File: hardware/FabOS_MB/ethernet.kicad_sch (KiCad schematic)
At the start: 40 parts, among them J301 RJ45, U301 LAN8742A, U302 CND-tek B1601S, U303 USBLC6-4SC6, Y301 Crystal_GND24

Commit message: routage
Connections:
- net Earth: no longer C311.2, U303.2 (GND)
- net GND: now also C311.2, U303.2 (GND)
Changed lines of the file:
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@@
-	)
-	(symbol
-		(lib_id "power:Earth")
-		(at 215.9 50.8 0)
-		(unit 1)
-		(exclude_from_sim no)
-		(in_bom yes)
-		(on_board yes)
-		(dnp no)
-		(property "Reference" "#PWR0314"
-			(at 215.9 57.15 0)
-			(effects
-				(font
-					(size 1.27 1.27)
-				)
-				(hide yes)
-			)
-		)
-		(property "Value" "Earth"
-			(at 219.71 49.276 90)
-			(effects
-				(font
-					(size 1.27 1.27)
-				)
-				(justify right)
-			)
-		)
-		(property "Footprint" ""
-			(at 215.9 50.8 0)
-			(effects
-				(font
-					(size 1.27 1.27)
-				)
-				(hide yes)
-			)
-		)
-		(property "Datasheet" "~"
-			(at 215.9 50.8 0)
-			(effects
-				(font
-					(size 1.27 1.27)
-				)
-				(hide yes)
-			)
-		)
-		(property "Description" "Power symbol creates a global label with name \"Earth\""
-			(at 215.9 50.8 0)
-			(effects
-				(font
-					(size 1.27 1.27)
-				)
-				(hide yes)
-			)
-		)
-		(pin "1"
-		)
-		(instances
-			(project "FabOS_MB"
-				(path "/09377d5d-727f-4ff4-92c8-7a0483d23f1e/97c1e665-4fec-464e-b9f4-4fa619e0ae43"
-					(reference "#PWR0314")
-					(unit 1)
-				)
-			)
-		)
 	)
 	(symbol
@@
 					(unit 1)
 				)
+			)
+		)
+	)
+	(symbol
+		(lib_id "power:GND")
+		(at 215.9 50.8 0)
+		(unit 1)
+		(exclude_from_sim no)
+		(in_bom yes)
+		(on_board yes)
+		(dnp no)
+		(fields_autoplaced yes)
+		(property "Reference" "#PWR0314"
+			(at 215.9 57.15 0)
+			(effects
+				(font
+					(size 1.27 1.27)
+				)
+				(hide yes)
+			)
+		)
+		(property "Value" "GND"
+			(at 215.9 55.88 0)
+			(effects
+				(font
+					(size 1.27 1.27)
+				)
+			)
+		)
+		(property "Footprint" ""
+			(at 215.9 50.8 0)
+			(effects
+				(font
+					(size 1.27 1.27)
+				)
+				(hide yes)
+			)
+		)
+		(property "Datasheet" ""
+			(at 215.9 50.8 0)
+			(effects
+				(font
+					(size 1.27 1.27)
+				)
+				(hide yes)
+			)
+		)
+		(property "Description" "Power symbol creates a global label with name \"GND\" , ground"
+			(at 215.9 50.8 0)
+			(effects
+				(font
+					(size 1.27 1.27)
+				)
+				(hide yes)
+			)
+		)
+		(pin "1"
+		)
+		(instances
+			(project "FabOS_MB"
+				(path "/09377d5d-727f-4ff4-92c8-7a0483d23f1e/97c1e665-4fec-464e-b9f4-4fa619e0ae43"
+					(reference "#PWR0314")
+					(unit 1)
+				)

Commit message: update
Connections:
- net Earth: now also C311.2, U303.2 (GND)
- net GND: no longer C311.2, U303.2 (GND)
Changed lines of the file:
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@@
+	)
+	(symbol
+		(lib_id "power:Earth")
+		(at 215.9 50.8 0)
+		(unit 1)
+		(exclude_from_sim no)
+		(in_bom yes)
+		(on_board yes)
+		(dnp no)
+		(property "Reference" "#PWR0314"
+			(at 215.9 57.15 0)
+			(effects
+				(font
+					(size 1.27 1.27)
+				)
+				(hide yes)
+			)
+		)
+		(property "Value" "Earth"
+			(at 219.71 49.276 90)
+			(effects
+				(font
+					(size 1.27 1.27)
+				)
+				(justify right)
+			)
+		)
+		(property "Footprint" ""
+			(at 215.9 50.8 0)
+			(effects
+				(font
+					(size 1.27 1.27)
+				)
+				(hide yes)
+			)
+		)
+		(property "Datasheet" "~"
+			(at 215.9 50.8 0)
+			(effects
+				(font
+					(size 1.27 1.27)
+				)
+				(hide yes)
+			)
+		)
+		(property "Description" "Power symbol creates a global label with name \"Earth\""
+			(at 215.9 50.8 0)
+			(effects
+				(font
+					(size 1.27 1.27)
+				)
+				(hide yes)
+			)
+		)
+		(pin "1"
+		)
+		(instances
+			(project "FabOS_MB"
+				(path "/09377d5d-727f-4ff4-92c8-7a0483d23f1e/97c1e665-4fec-464e-b9f4-4fa619e0ae43"
+					(reference "#PWR0314")
+					(unit 1)
+				)
+			)
+		)
 	)
 	(symbol
@@
 		(lib_id "Device:C_Small")
 		(at 97.79 36.83 0)
+		(mirror y)
 		(unit 1)
 		(exclude_from_sim no)
@@
 		(dnp no)
 		(property "Reference" "C306"
-			(at 100.33 35.56 0)
+			(at 95.25 35.56 0)
 			(effects
 				(font
@@
 		)
 		(property "Value" "100n"
-			(at 100.33 38.1 0)
+			(at 95.25 38.1 0)
 			(effects
 				(font
@@
 					(unit 1)
 				)
-			)
-		)
-	)
-	(symbol
-		(lib_id "power:GND")
-		(at 215.9 50.8 0)
-		(unit 1)
-		(exclude_from_sim no)
-		(in_bom yes)
-		(on_board yes)
-		(dnp no)
-		(fields_autoplaced yes)
-		(property "Reference" "#PWR0314"
-			(at 215.9 57.15 0)
-			(effects
-				(font
-					(size 1.27 1.27)
-				)
-				(hide yes)
-			)
-		)
-		(property "Value" "GND"
-			(at 215.9 55.88 0)
-			(effects
-				(font
-					(size 1.27 1.27)
-				)
-			)
-		)
-		(property "Footprint" ""
-			(at 215.9 50.8 0)
-			(effects
-				(font
-					(size 1.27 1.27)
-				)
-				(hide yes)
-			)
-		)
-		(property "Datasheet" ""
-			(at 215.9 50.8 0)
-			(effects
-				(font
-					(size 1.27 1.27)
-				)
-				(hide yes)
-			)
-		)
-		(property "Description" "Power symbol creates a global label with name \"GND\" , ground"
-			(at 215.9 50.8 0)
-			(effects
-				(font
-					(size 1.27 1.27)
-				)
-				(hide yes)
-			)
-		)
-		(pin "1"
-		)
-		(instances
-			(project "FabOS_MB"
-				(path "/09377d5d-727f-4ff4-92c8-7a0483d23f1e/97c1e665-4fec-464e-b9f4-4fa619e0ae43"
-					(reference "#PWR0314")
-					(unit 1)
-				)

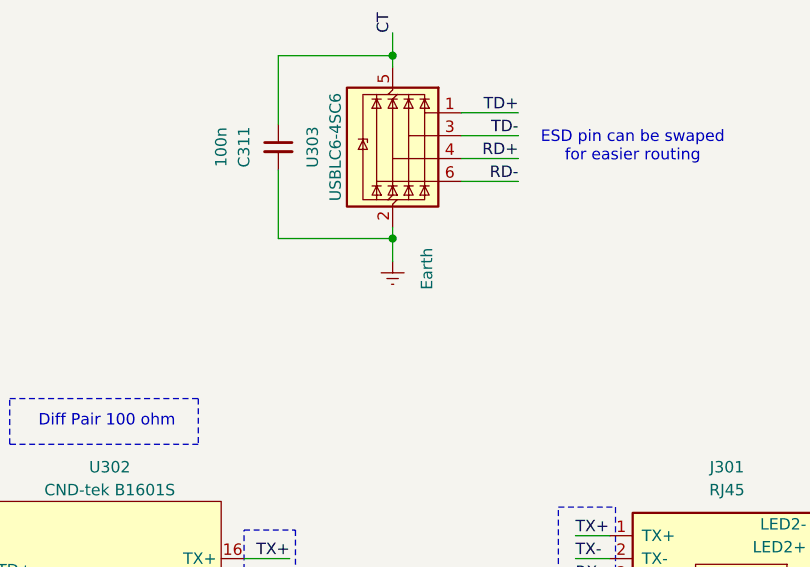
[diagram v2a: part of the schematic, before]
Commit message: update pcb
Tout les pins sont connectés. Il reste 32 violations à résoudre
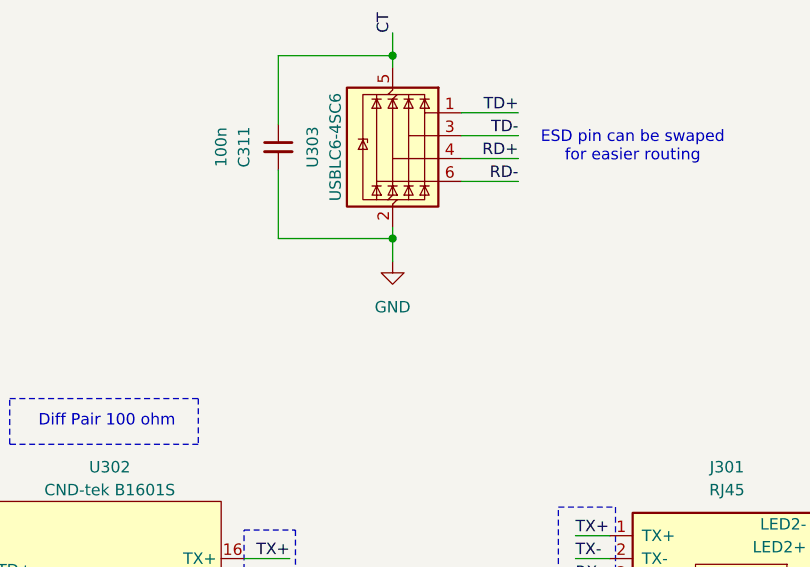
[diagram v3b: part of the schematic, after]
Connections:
- net Earth: no longer C311.2, U303.2 (GND)
- net GND: now also C311.2, U303.2 (GND)
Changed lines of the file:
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@@
-	)
-	(symbol
-		(lib_id "power:Earth")
-		(at 215.9 50.8 0)
-		(unit 1)
-		(exclude_from_sim no)
-		(in_bom yes)
-		(on_board yes)
-		(dnp no)
-		(property "Reference" "#PWR0314"
-			(at 215.9 57.15 0)
-			(effects
-				(font
-					(size 1.27 1.27)
-				)
-				(hide yes)
-			)
-		)
-		(property "Value" "Earth"
-			(at 219.71 49.276 90)
-			(effects
-				(font
-					(size 1.27 1.27)
-				)
-				(justify right)
-			)
-		)
-		(property "Footprint" ""
-			(at 215.9 50.8 0)
-			(effects
-				(font
-					(size 1.27 1.27)
-				)
-				(hide yes)
-			)
-		)
-		(property "Datasheet" "~"
-			(at 215.9 50.8 0)
-			(effects
-				(font
-					(size 1.27 1.27)
-				)
-				(hide yes)
-			)
-		)
-		(property "Description" "Power symbol creates a global label with name \"Earth\""
-			(at 215.9 50.8 0)
-			(effects
-				(font
-					(size 1.27 1.27)
-				)
-				(hide yes)
-			)
-		)
-		(pin "1"
-		)
-		(instances
-			(project "FabOS_MB"
-				(path "/09377d5d-727f-4ff4-92c8-7a0483d23f1e/97c1e665-4fec-464e-b9f4-4fa619e0ae43"
-					(reference "#PWR0314")
-					(unit 1)
-				)
-			)
-		)
 	)
 	(symbol
@@
 					(unit 1)
 				)
+			)
+		)
+	)
+	(symbol
+		(lib_id "power:GND")
+		(at 215.9 50.8 0)
+		(unit 1)
+		(exclude_from_sim no)
+		(in_bom yes)
+		(on_board yes)
+		(dnp no)
+		(fields_autoplaced yes)
+		(property "Reference" "#PWR0314"
+			(at 215.9 57.15 0)
+			(effects
+				(font
+					(size 1.27 1.27)
+				)
+				(hide yes)
+			)
+		)
+		(property "Value" "GND"
+			(at 215.9 55.88 0)
+			(effects
+				(font
+					(size 1.27 1.27)
+				)
+			)
+		)
+		(property "Footprint" ""
+			(at 215.9 50.8 0)
+			(effects
+				(font
+					(size 1.27 1.27)
+				)
+				(hide yes)
+			)
+		)
+		(property "Datasheet" ""
+			(at 215.9 50.8 0)
+			(effects
+				(font
+					(size 1.27 1.27)
+				)
+				(hide yes)
+			)
+		)
+		(property "Description" "Power symbol creates a global label with name \"GND\" , ground"
+			(at 215.9 50.8 0)
+			(effects
+				(font
+					(size 1.27 1.27)
+				)
+				(hide yes)
+			)
+		)
+		(pin "1"
+		)
+		(instances
+			(project ""
+				(path "/09377d5d-727f-4ff4-92c8-7a0483d23f1e/97c1e665-4fec-464e-b9f4-4fa619e0ae43"
+					(reference "#PWR0314")
+					(unit 1)
+				)

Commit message: Modification PCB
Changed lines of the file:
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@@
 	(wire
 		(pts
+			(xy 88.9 20.32) (xy 88.9 33.02)
+		)
+		(stroke
+			(width 0)
+			(type default)
+		)
+	)
+	(wire
+		(pts
 			(xy 72.39 93.98) (xy 76.2 93.98)
 		)
@@
 	(symbol
 		(lib_id "power:PWR_FLAG")
-		(at 88.9 33.02 180)
+		(at 88.9 20.32 0)
 		(unit 1)
 		(exclude_from_sim no)
@@
 		(fields_autoplaced yes)
 		(property "Reference" "#FLG0302"
-			(at 88.9 34.925 0)
+			(at 88.9 18.415 0)
 			(effects
 				(font
@@
 		)
 		(property "Value" "PWR_FLAG"
-			(at 88.9 38.1 0)
+			(at 88.9 15.24 0)
 			(effects
 				(font
@@
 		)
 		(property "Footprint" ""
-			(at 88.9 33.02 0)
+			(at 88.9 20.32 0)
 			(effects
 				(font
@@
 		)
 		(property "Datasheet" "~"
-			(at 88.9 33.02 0)
+			(at 88.9 20.32 0)
 			(effects
 				(font
@@
 		)
 		(property "Description" "Special symbol for telling ERC where power comes from"
-			(at 88.9 33.02 0)
+			(at 88.9 20.32 0)
 			(effects
 				(font

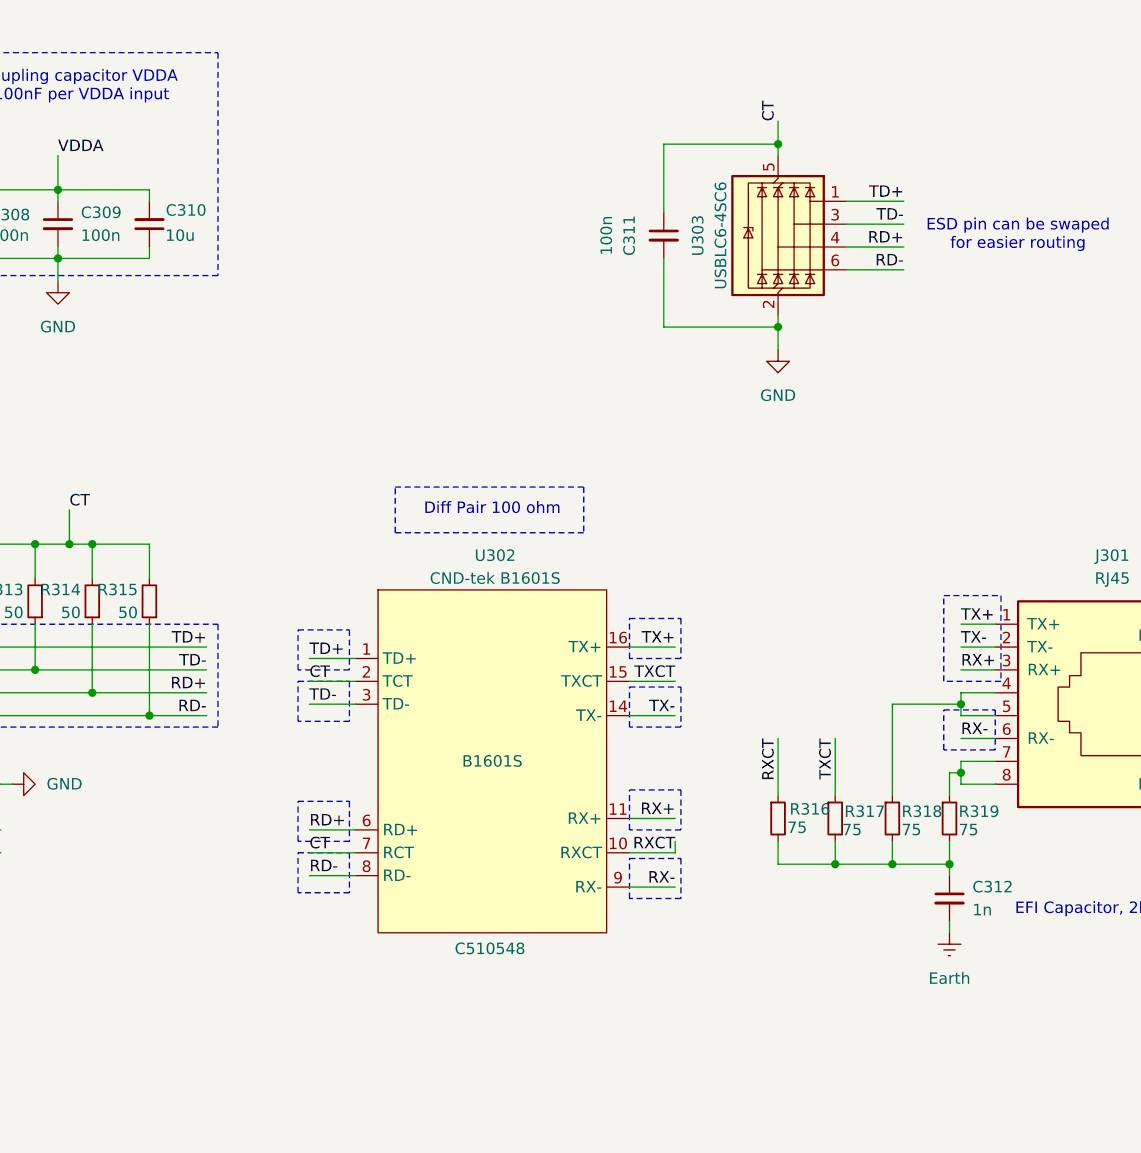
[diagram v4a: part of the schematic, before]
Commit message: update pcb routing
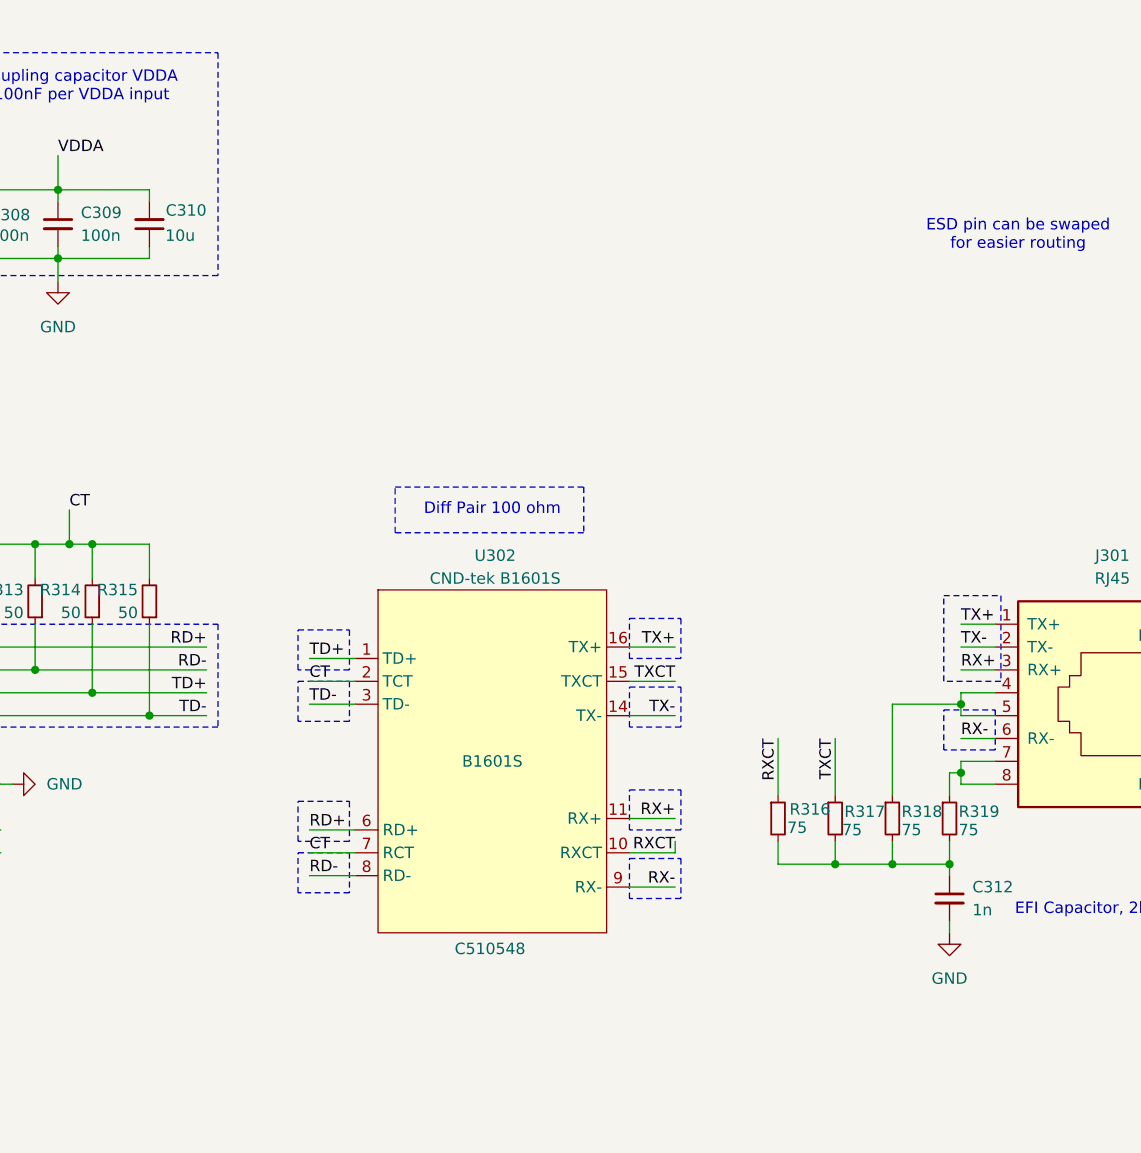
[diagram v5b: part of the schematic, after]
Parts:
- removed C311: 100n, Capacitor_SMD:C_0402_1005Metric, symbol Device:C_Small
- removed U303: USBLC6-4SC6, Package_TO_SOT_SMD:SOT-23-6, symbol Power_Protection:USBLC6-4SC6
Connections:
- net Earth is gone; now on net GND: C312.2
- net RD+: now also R311.2, U301.21 (TXP); no longer R314.1, U301.23 (RXP)
- net RD-: now also R313.1, U301.20 (TXN); no longer R315.1, U301.22 (RXN)
- net TD+: now also R314.1, U301.23 (RXP); no longer R311.2, U301.21 (TXP)
- net TD-: now also R315.1, U301.22 (RXN); no longer R313.1, U301.20 (TXN)

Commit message: update pcb
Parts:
- J301: LCSC (none) -> C20417896; MPN (none) -> HC-RJ45-5JAS-1-5-01
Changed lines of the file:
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@@
+			)
+		)
+		(property "MPN" "HC-RJ45-5JAS-1-5-01"
+			(at 255.27 88.9 0)
+			(effects
+				(font
+					(size 1.27 1.27)
+				)
+				(hide yes)
+			)
+		)
+		(property "LCSC" "C20417896"
+			(at 255.27 88.9 0)
+			(effects
+				(font
+					(size 1.27 1.27)
+				)
+				(hide yes)
 			)
 		)

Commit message: MàJ BoM dans Kicad
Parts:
- C301: LCSC (none) -> C147529
- C302: LCSC (none) -> C113791
- C303, C305: LCSC (none) -> C107000
- C304, C306, C307, C308, C309: LCSC (none) -> C361203
- C312: LCSC (none) -> C92841
- R301, R302, R303, R305: LCSC (none) -> C138002
- R304: LCSC (none) -> C114759
- R306, R307, R308, R309, R310, R321: LCSC (none) -> C25744
- R311, R313, R314, R315: LCSC (none) -> C87044
- R312: LCSC (none) -> C3015830
- R316, R317, R318, R319: LCSC (none) -> C323700
- R320, R322: LCSC (none) -> C11429
- U301: LCSC (none) -> C621424
